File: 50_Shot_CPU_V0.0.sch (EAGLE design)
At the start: 74 parts, among them IC1 PIC24FJ128GA010, J1 J12, J10 22-23-2021, J11 22-23-2061, J12 A311422_nd, J13 22-23-2021, J14 22-23-2021, J3 22-23-2021, J4 22-23-2021, J5 22-23-2021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

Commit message: converted LED headers
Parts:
- removed C6: .01uF, rcl:C-USC0805
- removed J11: 22-23-2061, Mine:22-23-2061
- removed J6, J7, J8: 22-23-2021, Mine:22-23-2021
- added JP5, JP6: SHERLOCK_4PIN_RGT, Mine:SHERLOCK_4PIN_RGT
- added JP7, JP8, JP9: SHERLOCK_2PIN_RGT, Mine:SHERLOCK_2PIN_RGT
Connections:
- removed net ###: J11-1.S, J11-2.S, J11-3.S, J11-4.S
- removed net N$73: J8-1.S, R7.2
- removed net N$74: J7-1.S, R6.2
- removed net N$76: J6-1.S, R5.2
- new net N$2: JP7.1, R5.2
- new net N$6: JP8.1, R6.2
- new net N$9: JP9.1, R7.2
- new net RB0: IC1.PGD1/EMUD1/AN0/CN2/RB0, JP6.3
- new net RC1: IC1.T2CK/RC1, JP5.1
- new net RC2: IC1.T3CK/RC2, JP5.2
- new net RC3: IC1.T4CK/RC3, JP5.3
- new net RC4: IC1.T5CK/RC4, JP5.4
- new net RE5: IC1.PMD5/RE5, JP6.4
- new net RE8: IC1.INT1/RE8, JP6.2
- new net RE9: IC1.INT2/RE9, JP6.1
- net GND: now also JP7.2, JP8.2, JP9.2; no longer C6.2, J11-5.S, J6-2.S, J7-2.S, J8-2.S
- net VDD: no longer C6.1, IC1.INT1/RE8, J11-6.S
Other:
- note added: "Expansion Header A"
- note added: "Expansion Header B"
- note removed: "Expansion Header"
- moved on the sheet: C7, JP4

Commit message: Added EEPROM to schematic
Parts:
- removed J10, J9: 22-23-2021, Mine:22-23-2021
- added C6: .01uf, rcl:C-USC0805
- added IC2: 93LC46ST, microchip:93LC46ST
- added JP10, JP11: SHERLOCK_2PIN_RGT, Mine:SHERLOCK_2PIN_RGT
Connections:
- removed net N$70: J10-1.S, R9.2
- removed net N$72: J9-1.S, R8.2
- new net N$12: JP10.1, R8.2
- new net N$13: JP11.1, R9.2
- new net RB10: IC1.PMA13/CVREF/AN10/RB10, IC2.DO
- new net RB11: IC1.PMA12/AN11/RB11, IC2.DI
- new net RB8: IC1.C1OUT/AN8/RB8, IC2.CS
- new net RB9: IC1.C2OUT/AN9/RB9, IC2.CLK
- new net RG15: IC1.RG15, IC2.ORG
- net GND: now also C6.2, IC2.GND, JP10.2, JP11.2; no longer J10-2.S, J9-2.S
- net VDD: now also C6.1, IC2.VCC
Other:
- note removed: "Adding this text, pushing, deleting from laptop, pulling"
- note removed: "it worked, try yhis again"
- moved on the sheet: C17

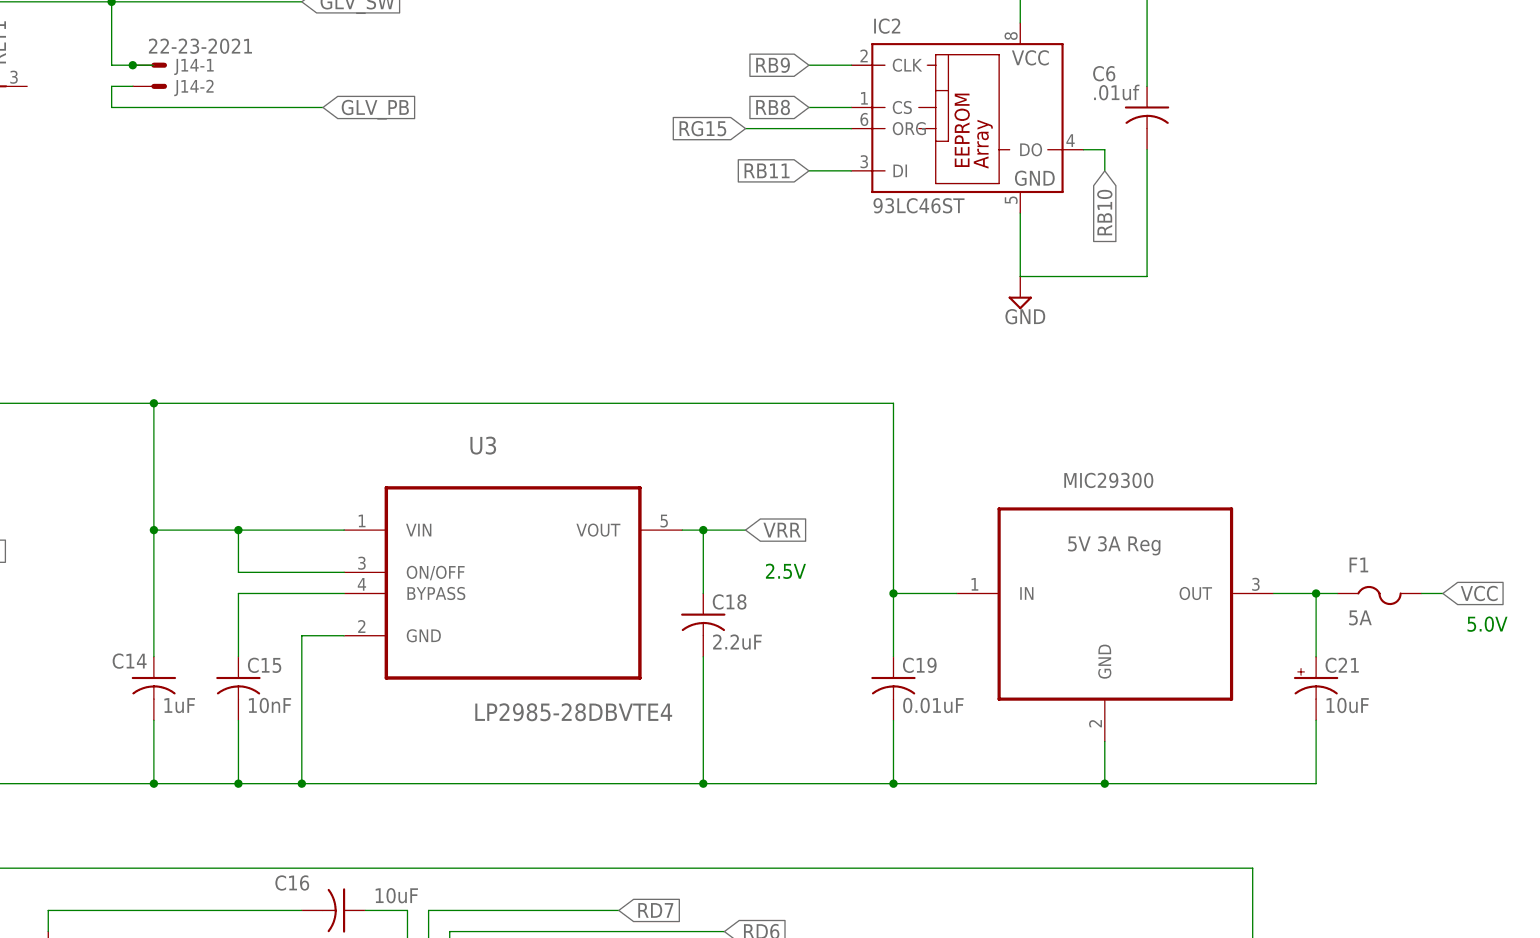
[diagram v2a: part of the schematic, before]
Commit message: Removed 5V reg and parts
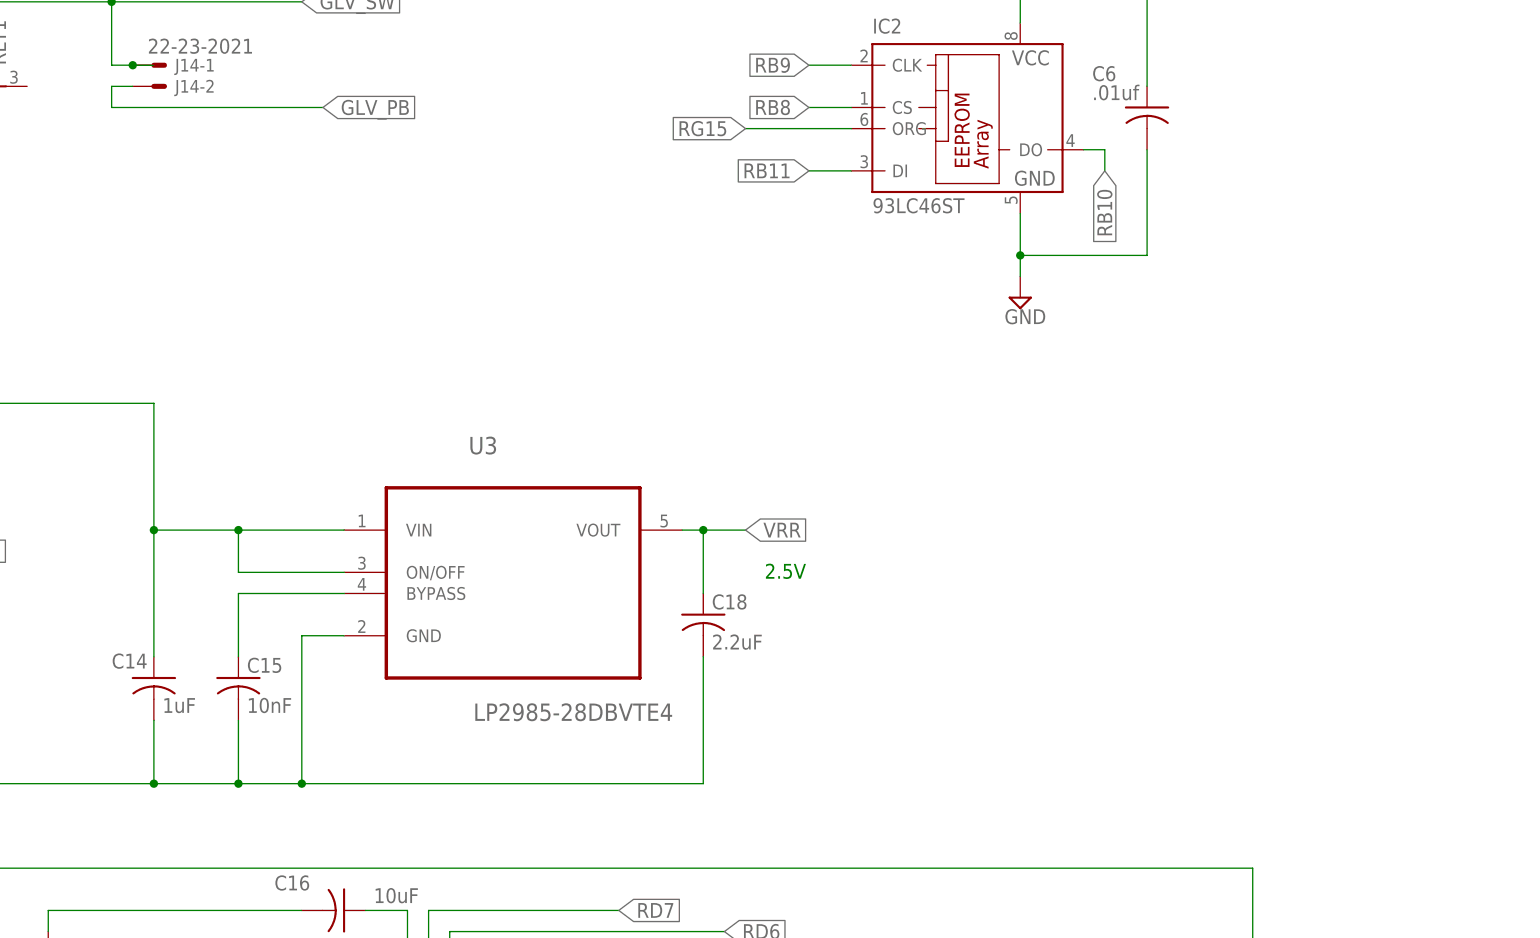
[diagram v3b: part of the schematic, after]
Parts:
- removed C19: 0.01uF, rcl:C-USC0805
- removed C21: 10uF, Mine:CAP3X3
- removed F1: 5A, Mine:FUSE_5X20
- removed U4: MIC29300, linear:MIC29300
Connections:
- removed net N$60: C21.+, F1.1, U4.OUT
- removed net VCC: F1.2
- net +12V: no longer C19.1, U4.IN
- net GND: no longer C19.2, C21.-, U4.GND
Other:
- note removed: "5.0V"
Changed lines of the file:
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@@
 <part name="C9" library="rcl" deviceset="C-US" device="C0805" value="1uF"/>
 <part name="SUPPLY6" library="supply2" deviceset="GND" device=""/>
-<part name="C19" library="rcl" deviceset="C-US" device="C0805" value="0.01uF"/>
 <part name="IC1" library="microchip" deviceset="PIC24FJ*GA010" device="" technology="128"/>
 <part name="R13" library="rcl-2" deviceset="R-US_" device="M0805" value="10k"/>
-<part name="C21" library="Mine" deviceset="CAP3X3" device="" value="10uF"/>
 <part name="S1" library="Mine" deviceset="TACT_PB" device=""/>
 <part name="C12" library="rcl" deviceset="C-US" device="C0805" value="0.1uF"/>
@@
 <part name="R12" library="rcl" deviceset="R-US_" device="M0805" value="10k"/>
 <part name="SUPPLY4" library="supply2" deviceset="GND" device=""/>
-<part name="U4" library="linear" deviceset="MIC29300" device=""/>
 <part name="J5" library="Mine" deviceset="22-23-2021" device=""/>
 <part name="R11" library="rcl" deviceset="R-US_" device="M0805" value="10k"/>
@@
 <part name="R8" library="rcl" deviceset="R-US_" device="M0805" value="330"/>
 <part name="R9" library="rcl" deviceset="R-US_" device="M0805" value="330"/>
-<part name="F1" library="Mine" deviceset="FUSE_5X20" device="" value="5A"/>
 <part name="J1" library="Mine" deviceset="22-23-2061" device="" value="J12"/>
 <part name="R4" library="rcl" deviceset="R-US_" device="M0805" value="10k"/>
@@
 <part name="SUPPLY5" library="supply2" deviceset="GND" device=""/>
 <part name="IC2" library="microchip" deviceset="93*" device="ST" technology="LC46"/>
-<part name="SUPPLY14" library="supply2" deviceset="GND" device=""/>
 <part name="C6" library="rcl" deviceset="C-US" device="C0805" value=".01uf"/>
+<part name="SUPPLY15" library="supply2" deviceset="GND" device=""/>
 </parts>
 <sheets>
@@
 <plain>
 <text x="81.28" y="127.508" size="1.778" layer="91">3.3V</text>
-<text x="264.414" y="122.428" size="1.778" layer="91">5.0V</text>
 <text x="14.224" y="9.144" size="1.778" layer="91" rot="R90">Reset</text>
 <text x="180.086" y="128.778" size="1.778" layer="91">2.5V</text>
@@
 <attribute name="VALUE" x="26.035" y="98.425" size="1.778" layer="96"/>
 </instance>
-<instance part="C19" gate="G$1" x="195.58" y="116.84" smashed="yes">
-<attribute name="NAME" x="196.596" y="117.475" size="1.778" layer="95"/>
-<attribute name="VALUE" x="196.596" y="112.649" size="1.778" layer="96"/>
-</instance>
 <instance part="IC1" gate="G$1" x="129.54" y="20.32" smashed="yes">
 <attribute name="NAME" x="63.5" y="57.15" size="1.778" layer="95"/>
@@
 <attribute name="NAME" x="13.7414" y="34.29" size="1.778" layer="95" rot="R90"/>
 <attribute name="VALUE" x="18.542" y="34.29" size="1.778" layer="96" rot="R90"/>
-</instance>
-<instance part="C21" gate="G$1" x="251.46" y="114.3" smashed="yes">
-<attribute name="NAME" x="247.396" y="117.475" size="1.778" layer="95"/>
-<attribute name="VALUE" x="247.396" y="112.649" size="1.778" layer="96"/>
 </instance>
 <instance part="S1" gate="G$1" x="15.24" y="5.08" smashed="yes" rot="R90">
@@
 <attribute name="VALUE" x="-100.965" y="-31.115" size="1.778" layer="96"/>
 </instance>
-<instance part="U4" gate="G$1" x="220.98" y="124.46" smashed="yes"/>
 <instance part="J5" gate="-1" x="-121.92" y="91.44" smashed="yes">
 <attribute name="NAME" x="-119.38" y="90.678" size="1.524" layer="95"/>
@@
 <attribute name="VALUE" x="-100.584" y="-14.732" size="1.778" layer="96" rot="R180"/>
 </instance>
-<instance part="F1" gate="G$1" x="254" y="127"/>
 <instance part="J1" gate="-1" x="-154.94" y="139.7"/>
 <instance part="J1" gate="-2" x="-154.94" y="137.16"/>
@@
 </instance>
 <instance part="IC2" gate="G$1" x="203.2" y="182.88"/>
-<instance part="SUPPLY14" gate="GND" x="210.82" y="162.56" smashed="yes">
-<attribute name="VALUE" x="208.915" y="159.385" size="1.778" layer="96"/>
-</instance>
 <instance part="C6" gate="G$1" x="226.06" y="185.42" smashed="yes">
 <attribute name="NAME" x="219.456" y="188.595" size="1.778" layer="95"/>
 <attribute name="VALUE" x="219.456" y="186.309" size="1.778" layer="96"/>
+</instance>
+<instance part="SUPPLY15" gate="GND" x="210.82" y="162.56" smashed="yes">
+<attribute name="VALUE" x="208.915" y="159.385" size="1.778" layer="96"/>
 </instance>
 </instances>
@@
 </segment>
 <segment>
-<pinref part="C19" gate="G$1" pin="1"/>
-<wire x1="203.2" y1="127" x2="195.58" y2="127" width="0.1524" layer="91"/>
-<wire x1="195.58" y1="127" x2="195.58" y2="119.38" width="0.1524" layer="91"/>
 <wire x1="15.24" y1="149.86" x2="106.68" y2="149.86" width="0.1524" layer="91"/>
-<wire x1="106.68" y1="149.86" x2="195.58" y2="149.86" width="0.1524" layer="91"/>
-<wire x1="195.58" y1="149.86" x2="195.58" y2="127" width="0.1524" layer="91"/>
-<junction x="195.58" y="127"/>
-<pinref part="U4" gate="G$1" pin="IN"/>
 <wire x1="15.24" y1="134.62" x2="15.24" y2="149.86" width="0.1524" layer="91"/>
 <junction x="15.24" y="149.86"/>
@@
 <wire x1="106.68" y1="134.62" x2="106.68" y2="149.86" width="0.1524" layer="91"/>
 <junction x="106.68" y="134.62"/>
-<junction x="106.68" y="149.86"/>
 <wire x1="15.24" y1="149.86" x2="15.24" y2="152.4" width="0.1524" layer="91"/>
 <label x="15.24" y="152.4" size="1.778" layer="95" rot="R90" xref="yes"/>
@@
 <wire x1="15.24" y1="109.22" x2="15.24" y2="104.14" width="0.1524" layer="91"/>
 <junction x="15.24" y="104.14"/>
-<wire x1="220.98" y1="109.22" x2="220.98" y2="104.14" width="0.1524" layer="91"/>
-<wire x1="220.98" y1="104.14" x2="195.58" y2="104.14" width="0.1524" layer="91"/>
 <junction x="68.58" y="104.14"/>
-<pinref part="C19" gate="G$1" pin="2"/>
-<wire x1="195.58" y1="104.14" x2="172.72" y2="104.14" width="0.1524" layer="91"/>
 <wire x1="172.72" y1="104.14" x2="124.46" y2="104.14" width="0.1524" layer="91"/>
 <wire x1="124.46" y1="104.14" x2="116.84" y2="104.14" width="0.1524" layer="91"/>
 <wire x1="116.84" y1="104.14" x2="106.68" y2="104.14" width="0.1524" layer="91"/>
 <wire x1="106.68" y1="104.14" x2="68.58" y2="104.14" width="0.1524" layer="91"/>
-<wire x1="195.58" y1="111.76" x2="195.58" y2="104.14" width="0.1524" layer="91"/>
-<junction x="195.58" y="104.14"/>
-<wire x1="246.38" y1="111.76" x2="246.38" y2="104.14" width="0.1524" layer="91"/>
-<wire x1="246.38" y1="104.14" x2="220.98" y2="104.14" width="0.1524" layer="91"/>
-<junction x="220.98" y="104.14"/>
-<pinref part="C21" gate="G$1" pin="-"/>
-<pinref part="U4" gate="G$1" pin="GND"/>
 <pinref part="U2" gate="A" pin="GND"/>
 <pinref part="U3" gate="A" pin="GND"/>
@@
 <pinref part="C18" gate="G$1" pin="2"/>
 <wire x1="172.72" y1="119.38" x2="172.72" y2="104.14" width="0.1524" layer="91"/>
-<junction x="172.72" y="104.14"/>
 <pinref part="J13" gate="-2" pin="S"/>
 <wire x1="5.08" y1="147.32" x2="10.16" y2="147.32" width="0.1524" layer="91"/>
@@
 <segment>
 <pinref part="IC2" gate="G$1" pin="GND"/>
-<wire x1="210.82" y1="172.72" x2="210.82" y2="165.1" width="0.1524" layer="91"/>
-<pinref part="SUPPLY14" gate="GND" pin="GND"/>
+<wire x1="210.82" y1="172.72" x2="210.82" y2="167.64" width="0.1524" layer="91"/>
 <pinref part="C6" gate="G$1" pin="2"/>
-<wire x1="226.06" y1="180.34" x2="226.06" y2="165.1" width="0.1524" layer="91"/>
-<wire x1="226.06" y1="165.1" x2="210.82" y2="165.1" width="0.1524" layer="91"/>
-</segment>
-</net>
-<net name="VCC" class="0">
-<segment>
-<pinref part="F1" gate="G$1" pin="2"/>
-<wire x1="259.08" y1="127" x2="261.62" y2="127" width="0.1524" layer="91"/>
-<label x="261.62" y="127" size="1.778" layer="95" xref="yes"/>
+<wire x1="226.06" y1="180.34" x2="226.06" y2="167.64" width="0.1524" layer="91"/>
+<wire x1="226.06" y1="167.64" x2="210.82" y2="167.64" width="0.1524" layer="91"/>
+<wire x1="210.82" y1="167.64" x2="210.82" y2="165.1" width="0.1524" layer="91"/>
+<junction x="210.82" y="167.64"/>
+<pinref part="SUPPLY15" gate="GND" pin="GND"/>
 </segment>
 </net>
@@
 </segment>
 </net>
-<net name="N$60" class="0">
-<segment>
-<pinref part="C21" gate="G$1" pin="+"/>
-<wire x1="246.38" y1="119.38" x2="246.38" y2="127" width="0.1524" layer="91"/>
-<pinref part="U4" gate="G$1" pin="OUT"/>
-<wire x1="246.38" y1="127" x2="241.3" y2="127" width="0.1524" layer="91"/>
-<pinref part="F1" gate="G$1" pin="1"/>
-<wire x1="248.92" y1="127" x2="246.38" y2="127" width="0.1524" layer="91"/>
-<junction x="246.38" y="127"/>
-</segment>
-</net>
